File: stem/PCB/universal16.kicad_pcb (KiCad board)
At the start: 2 copper layers, 99.5 x 99.5 mm, 576 parts, among them J1 Conn_01x04, J11 Conn_01x01, J12 Conn_01x01, J13 Conn_01x01, J14 Conn_01x01, J2 Conn_01x04, J3 Conn_01x04, J4 Conn_01x04, J5 Conn_01x03, J6 Conn_01x03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

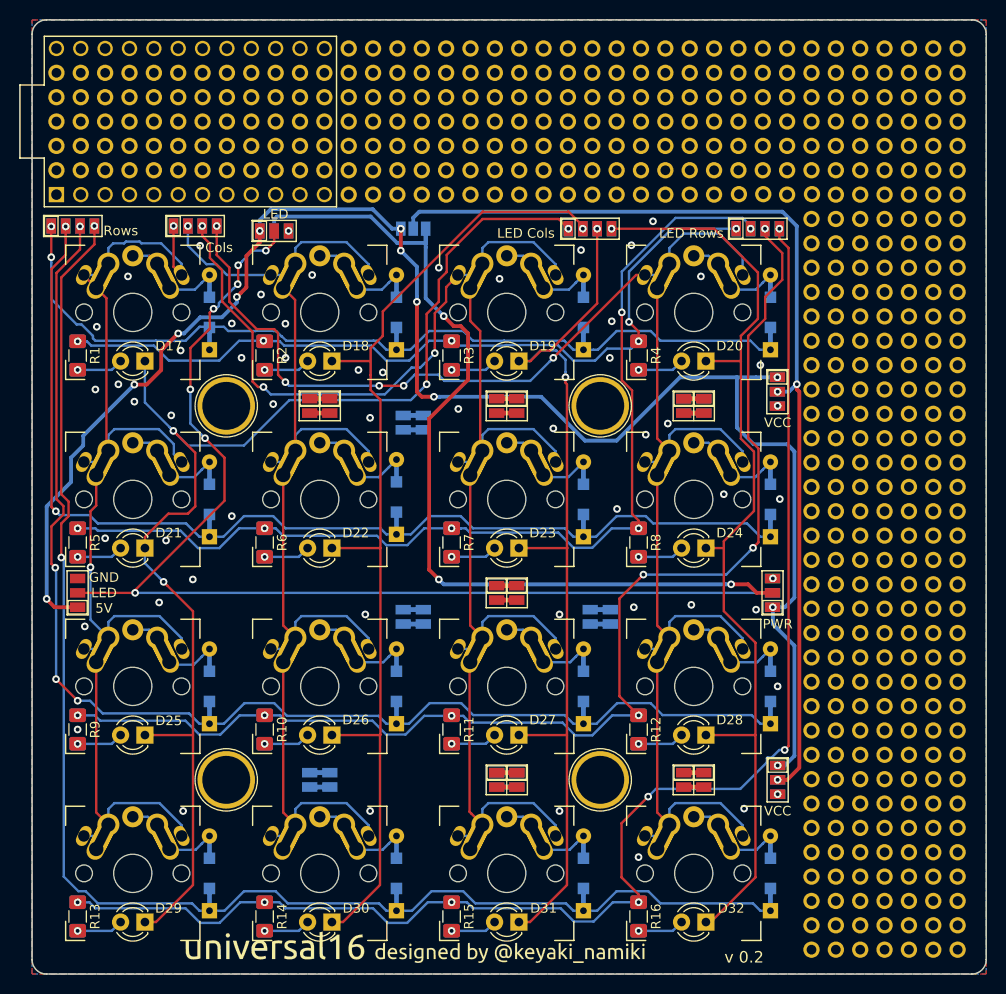
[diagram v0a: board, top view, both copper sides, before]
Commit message: redraw some wires
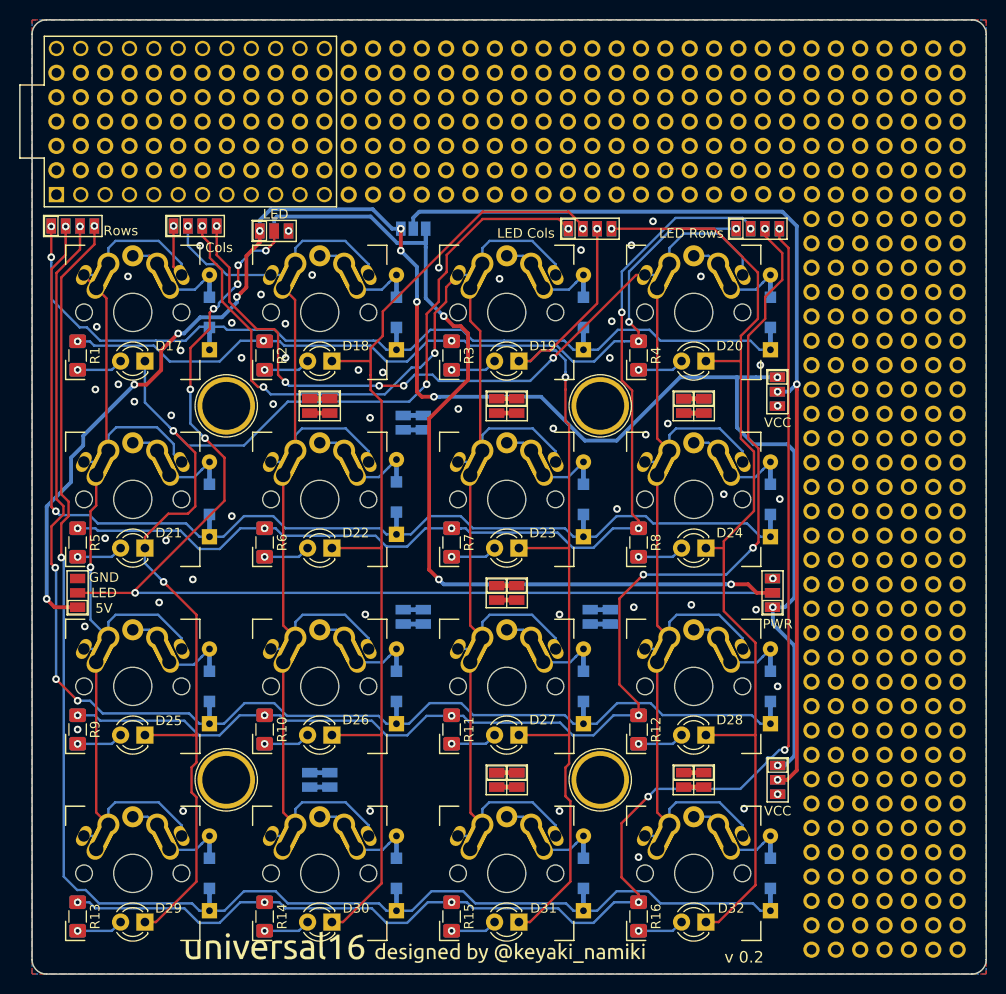
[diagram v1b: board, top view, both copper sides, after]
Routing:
- net LEDcol0: track 133.1 -> 134.5 mm
- net LEDcol2: track 95.7 -> 96.5 mm

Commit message: fix footprint compatibility
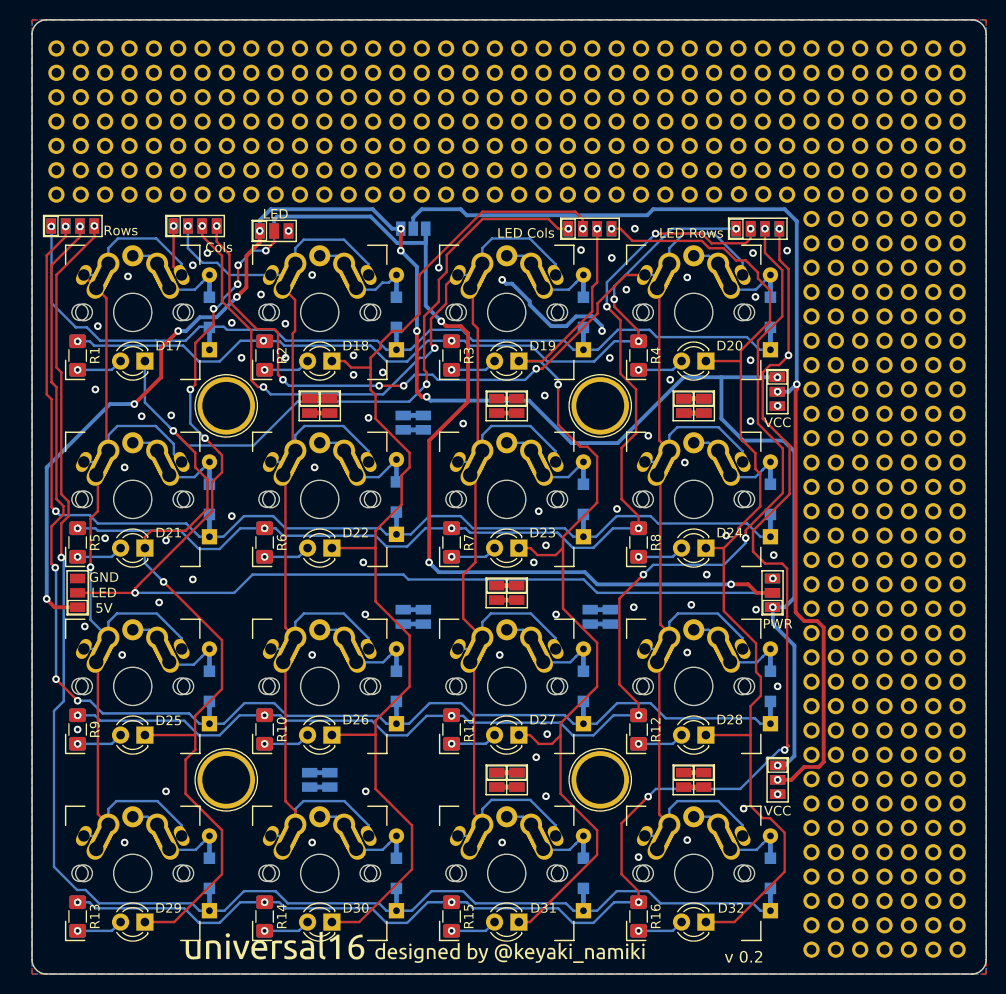
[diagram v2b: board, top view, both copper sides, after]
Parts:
- removed the REF** at (105.4, 71.1)
- added P?: CONN_1, keyboard_parts:PIN_1, F.Cu at (114.3, 78.7)
- added P?: CONN_1, keyboard_parts:PIN_1, F.Cu at (96.5, 76.2)
- added P?: CONN_1, keyboard_parts:PIN_1, F.Cu at (99.1, 76.2)
- added P?: CONN_1, keyboard_parts:PIN_1, F.Cu at (109.2, 76.2)
- added P?: CONN_1, keyboard_parts:PIN_1, F.Cu at (101.6, 76.2)
- added P?: CONN_1, keyboard_parts:PIN_1, F.Cu at (106.7, 76.2)
- added P?: CONN_1, keyboard_parts:PIN_1, F.Cu at (104.1, 76.2)
- added P?: CONN_1, keyboard_parts:PIN_1, F.Cu at (116.8, 76.2)
- added P?: CONN_1, keyboard_parts:PIN_1, F.Cu at (114.3, 76.2)
- added P?: CONN_1, keyboard_parts:PIN_1, F.Cu at (119.4, 76.2)
- added P?: CONN_1, keyboard_parts:PIN_1, F.Cu at (111.8, 76.2)
- added P?: CONN_1, keyboard_parts:PIN_1, F.Cu at (116.8, 78.7)
- added P?: CONN_1, keyboard_parts:PIN_1, F.Cu at (99.1, 78.7)
- added P?: CONN_1, keyboard_parts:PIN_1, F.Cu at (91.4, 78.7)
- added P?: CONN_1, keyboard_parts:PIN_1, F.Cu at (94.0, 78.7)
- added P?: CONN_1, keyboard_parts:PIN_1, F.Cu at (96.5, 78.7)
- added P?: CONN_1, keyboard_parts:PIN_1, F.Cu at (101.6, 78.7)
- added P?: CONN_1, keyboard_parts:PIN_1, F.Cu at (119.4, 78.7)
- added P?: CONN_1, keyboard_parts:PIN_1, F.Cu at (111.8, 78.7)
- added P?: CONN_1, keyboard_parts:PIN_1, F.Cu at (109.2, 78.7)
- added P?: CONN_1, keyboard_parts:PIN_1, F.Cu at (106.7, 78.7)
- added P?: CONN_1, keyboard_parts:PIN_1, F.Cu at (104.1, 78.7)
- added P?: CONN_1, keyboard_parts:PIN_1, F.Cu at (94.0, 76.2)
- added P?: CONN_1, keyboard_parts:PIN_1, F.Cu at (91.4, 76.2)
- moved P? 2.54 mm to (94.0, 63.5)
- moved P? 2.54 mm to (91.4, 63.5)
- moved P? 2.54 mm to (104.1, 63.5)
- moved P? 2.54 mm to (99.1, 63.5)
- moved P? 2.54 mm to (101.6, 63.5)
- moved P? 2.54 mm to (96.5, 63.5)
- moved P? 2.54 mm to (111.8, 63.5)
- moved P? 2.54 mm to (114.3, 63.5)
- moved P? 2.54 mm to (109.2, 63.5)
- moved P? 2.54 mm to (106.7, 63.5)
- moved P? 2.54 mm to (119.4, 68.6)
- moved P? 2.54 mm to (114.3, 68.6)
- moved P? 2.54 mm to (116.8, 68.6)
- moved P? 2.54 mm to (111.8, 68.6)
- moved P? 2.54 mm to (109.2, 68.6)
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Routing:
- net GND: track 0.00 -> 14.0 mm, vias 56 -> 78
- net LEDcol1: track 107.8 -> 117.5 mm
- net LEDcol0: track 134.5 -> 142.1 mm
- net LEDrow3: track 148.2 -> 155.1 mm, vias 7 -> 8
- net LEDcol2: track 96.5 -> 102.8 mm
- net LEDcol3: track 102.5 -> 108.4 mm
- net VCC: track 103.6 -> 109.0 mm
- net LEDrow1: track 107.4 -> 110.6 mm, vias 6 -> 7
- net col2: track 160.2 -> 162.2 mm
- net 5V: track 179.7 -> 181.3 mm
- net LED: track 120.1 -> 121.5 mm
- net LEDrow0: track 84.4 -> 85.7 mm
- net row3: track 150.2 -> 151.5 mm
- net col1: track 123.4 -> 124.3 mm
- net col0: track 119.9 -> 120.5 mm
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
